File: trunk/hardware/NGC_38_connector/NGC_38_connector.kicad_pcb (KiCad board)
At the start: 2 copper layers, 38 x 29 mm, 5 parts, among them P1 DIL38, P2 CONN_10, P3 CONN_9, P4 CONN_10, P5 CONN_9

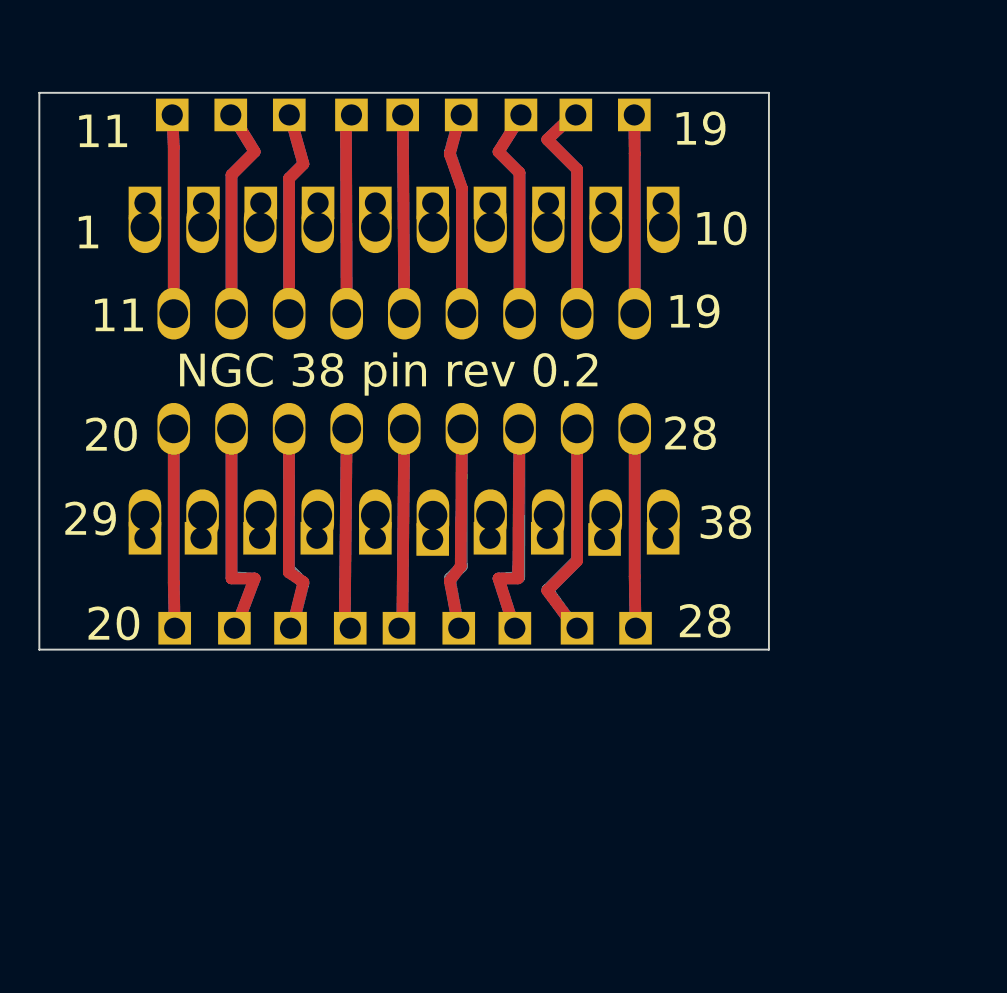
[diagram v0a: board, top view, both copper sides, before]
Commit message: 
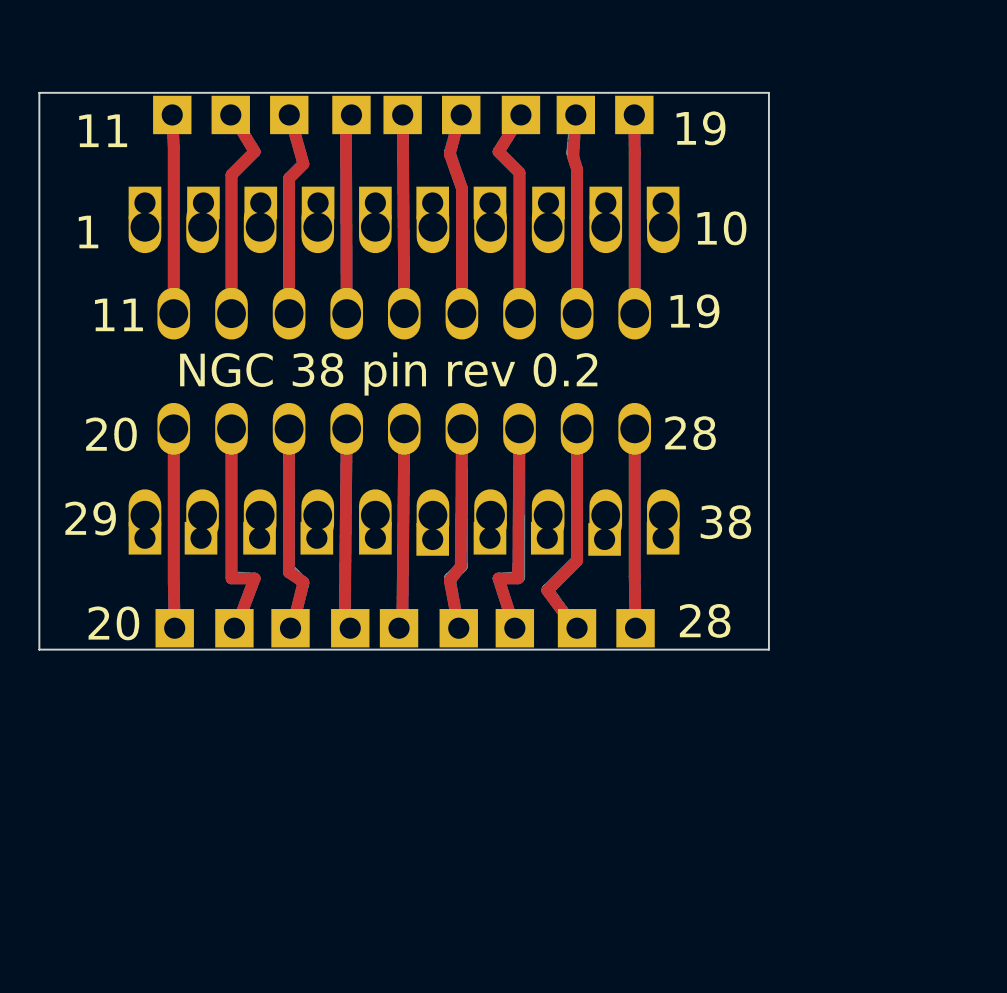
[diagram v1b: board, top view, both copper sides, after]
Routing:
- net N-0000013: track 23.5 -> 21.0 mm
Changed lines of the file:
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@@
     (links 38)
     (no_connects 0)
-    (area 130.949999 132.969 169.050001 165.061901)
+    (area 130.949999 132.969 169.050001 165.053714)
     (thickness 1.6)
     (drawings 30)
@@
     (mod_text_size 1 1)
     (mod_text_width 0.15)
-    (pad_size 1.7 1.7)
+    (pad_size 2 2)
     (pad_drill 1.1)
     (pad_to_mask_clearance 0)
@@
       (effects (font (size 1.524 1.016) (thickness 0.254)))
     )
-    (pad 1 thru_hole rect (at -11.684 0) (size 1.7 1.7) (drill 1.1)
+    (pad 1 thru_hole rect (at -11.684 0) (size 2 2) (drill 1.1)
       (layers *.Cu *.Mask F.SilkS)
       (net 8 N-0000016)
     )
-    (pad 2 thru_hole rect (at -8.5725 0) (size 1.7 1.7) (drill 1.1)
+    (pad 2 thru_hole rect (at -8.5725 0) (size 2 2) (drill 1.1)
       (layers *.Cu *.Mask F.SilkS)
       (net 21 N-0000028)
     )
-    (pad 3 thru_hole rect (at -5.6515 0) (size 1.7 1.7) (drill 1.1)
+    (pad 3 thru_hole rect (at -5.6515 0) (size 2 2) (drill 1.1)
       (layers *.Cu *.Mask F.SilkS)
       (net 20 N-0000027)
     )
-    (pad 4 thru_hole rect (at -2.54 0) (size 1.7 1.7) (drill 1.1)
+    (pad 4 thru_hole rect (at -2.54 0) (size 2 2) (drill 1.1)
       (layers *.Cu *.Mask F.SilkS)
       (net 19 N-0000026)
     )
-    (pad 5 thru_hole rect (at 0 0) (size 1.7 1.7) (drill 1.1)
+    (pad 5 thru_hole rect (at 0 0) (size 2 2) (drill 1.1)
       (layers *.Cu *.Mask F.SilkS)
       (net 18 N-0000025)
     )
-    (pad 6 thru_hole rect (at 3.1115 0) (size 1.7 1.7) (drill 1.1)
+    (pad 6 thru_hole rect (at 3.1115 0) (size 2 2) (drill 1.1)
       (layers *.Cu *.Mask F.SilkS)
       (net 17 N-0000024)
     )
-    (pad 7 thru_hole rect (at 6.0325 0) (size 1.7 1.7) (drill 1.1)
+    (pad 7 thru_hole rect (at 6.0325 0) (size 2 2) (drill 1.1)
       (layers *.Cu *.Mask F.SilkS)
       (net 16 N-0000023)
     )
-    (pad 8 thru_hole rect (at 9.271 0) (size 1.7 1.7) (drill 1.1)
+    (pad 8 thru_hole rect (at 9.271 0) (size 2 2) (drill 1.1)
       (layers *.Cu *.Mask F.SilkS)
       (net 15 N-0000022)
     )
-    (pad 9 thru_hole rect (at 12.319 0) (size 1.7 1.7) (drill 1.1)
+    (pad 9 thru_hole rect (at 12.319 0) (size 2 2) (drill 1.1)
       (layers *.Cu *.Mask F.SilkS)
       (net 14 N-0000021)
@@
       (effects (font (size 1.524 1.016) (thickness 0.254)))
     )
-    (pad 1 thru_hole rect (at -11.8745 0) (size 1.7 1.7) (drill 1.1)
+    (pad 1 thru_hole rect (at -11.8745 0) (size 2 2) (drill 1.1)
       (layers *.Cu *.Mask F.SilkS)
       (net 13 N-0000020)
     )
-    (pad 2 thru_hole rect (at -8.8265 0) (size 1.7 1.7) (drill 1.1)
+    (pad 2 thru_hole rect (at -8.8265 0) (size 2 2) (drill 1.1)
       (layers *.Cu *.Mask F.SilkS)
       (net 11 N-0000019)
     )
-    (pad 3 thru_hole rect (at -5.7785 0) (size 1.7 1.7) (drill 1.1)
+    (pad 3 thru_hole rect (at -5.7785 0) (size 2 2) (drill 1.1)
       (layers *.Cu *.Mask F.SilkS)
       (net 10 N-0000018)
     )
-    (pad 4 thru_hole rect (at -2.54 0) (size 1.7 1.7) (drill 1.1)
+    (pad 4 thru_hole rect (at -2.54 0) (size 2 2) (drill 1.1)
       (layers *.Cu *.Mask F.SilkS)
       (net 9 N-0000017)
     )
-    (pad 5 thru_hole rect (at 0.127 0) (size 1.7 1.7) (drill 1.1)
+    (pad 5 thru_hole rect (at 0.127 0) (size 2 2) (drill 1.1)
       (layers *.Cu *.Mask F.SilkS)
       (net 1 N-000001)
     )
-    (pad 6 thru_hole rect (at 3.175 0) (size 1.7 1.7) (drill 1.1)
+    (pad 6 thru_hole rect (at 3.175 0) (size 2 2) (drill 1.1)
       (layers *.Cu *.Mask F.SilkS)
       (net 7 N-0000015)
     )
-    (pad 7 thru_hole rect (at 6.2865 0) (size 1.7 1.7) (drill 1.1)
+    (pad 7 thru_hole rect (at 6.2865 0) (size 2 2) (drill 1.1)
       (layers *.Cu *.Mask F.SilkS)
       (net 6 N-0000014)
     )
-    (pad 8 thru_hole rect (at 9.144 0) (size 1.7 1.7) (drill 1.1)
+    (pad 8 thru_hole rect (at 9.144 0) (size 2 2) (drill 1.1)
       (layers *.Cu *.Mask F.SilkS)
       (net 5 N-0000013)
     )
-    (pad 9 thru_hole rect (at 12.192 0) (size 1.7 1.7) (drill 1.1)
+    (pad 9 thru_hole rect (at 12.192 0) (size 2 2) (drill 1.1)
       (layers *.Cu *.Mask F.SilkS)
       (net 4 N-0000012)
@@
   (segment (start 162.008 138.678) (end 161.9885 136.5885) (width 0.6096) (layer B.Cu) (net 4) (status 20))
   (segment (start 159.008 147) (end 159.008 139.488) (width 0.6096) (layer F.Cu) (net 5))
-  (segment (start 159.008 139.488) (end 157.455 137.935) (width 0.6096) (layer F.Cu) (net 5))
-  (segment (start 157.455 137.935) (end 158.9405 136.525) (width 0.6096) (layer F.Cu) (net 5) (status 20))
+  (segment (start 159.008 139.488) (end 158.8135 138.8745) (width 0.6096) (layer F.Cu) (net 5))
+  (segment (start 158.8135 138.8745) (end 158.9405 136.525) (width 0.6096) (layer F.Cu) (net 5) (status 20))
   (segment (start 159.008 147) (end 159.008 139.488) (width 0.6096) (layer B.Cu) (net 5))
-  (segment (start 157.455 137.935) (end 158.9405 136.525) (width 0.6096) (layer B.Cu) (net 5) (status 20))
-  (segment (start 159.008 139.488) (end 157.455 137.935) (width 0.6096) (layer B.Cu) (net 5))
+  (segment (start 158.75 138.6205) (end 158.9405 136.525) (width 0.6096) (layer B.Cu) (net 5) (status 20))
+  (segment (start 159.008 139.488) (end 158.75 138.6205) (width 0.6096) (layer B.Cu) (net 5))
   (segment (start 156.008 147) (end 156.008 139.663) (width 0.6096) (layer F.Cu) (net 6))
   (segment (start 156.008 139.663) (end 154.915 138.57) (width 0.6096) (layer F.Cu) (net 6))

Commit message: 0.3
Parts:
- moved P4 0.88 mm to (149.3, 159.6)
- moved P2 0.78 mm to (149.7, 140.5)
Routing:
- net N-0000022: track 23.3 -> 21.0 mm
- net N-0000023: track 23.2 -> 20.9 mm
- net N-0000036: track 0.00 -> 2.15 mm
- net N-0000030: track 0.00 -> 2.14 mm
- net N-0000034: track 0.00 -> 2.10 mm
- net N-0000031: track 0.00 -> 2.09 mm
- net N-0000035: track 0.00 -> 2.09 mm
- net N-0000032: track 0.00 -> 2.08 mm
- net N-0000037: track 0.00 -> 2.08 mm
- net N-0000033: track 0.00 -> 2.08 mm
- net N-0000029: track 0.00 -> 2.08 mm
- net N-0000038: track 0.00 -> 2.08 mm
- net N-0000010: track 0.00 -> 2.07 mm
- net N-000009: track 0.00 -> 2.06 mm
- net N-000004: track 0.00 -> 2.06 mm
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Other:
- board text added: "NGC 38 pin rev 0.3"
- board text removed: "NGC 38 pin rev 0.2"

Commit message: 4.0.1
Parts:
- added P6: CONN_10, SIL-10, F.Cu at (163.2, 134.6)
- added P7: CONN_9, SIL-9, F.Cu at (163.2, 141.0)
- added P8: CONN_9, SIL-9, F.Cu at (163.2, 172.1)
- added P9: CONN_10, SIL-10, F.Cu at (163.2, 178.4)
- moved P4 21.4 mm to (163.2, 175.9)
- moved P3 15.1 mm to (163.2, 143.5)
- moved P1 15.0 mm to (149.9, 156.8)
- moved P5 14.8 mm to (163.2, 169.5)
- moved P2 13.9 mm to (163.2, 137.2)
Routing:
- net N-0000010: track 2.04 -> 31.3 mm
- net N-000001: track 2.05 -> 31.0 mm
- net N-000009: track 2.05 -> 30.9 mm
- net N-000002: track 2.07 -> 30.6 mm
- net N-000008: track 2.06 -> 30.5 mm
- net N-000003: track 2.06 -> 30.3 mm
- net N-000007: track 2.04 -> 30.2 mm
- net N-0000035: track 2.08 -> 30.0 mm
- net N-000004: track 2.06 -> 29.9 mm
- net N-000006: track 2.04 -> 29.8 mm
- net N-0000027: track 2.09 -> 29.8 mm
- net N-0000034: track 2.15 -> 29.7 mm
- net N-000005: track 2.05 -> 29.5 mm
- net N-0000028: track 2.10 -> 29.4 mm
- net N-0000033: track 2.08 -> 29.3 mm
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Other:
- board size 38 x 29 mm -> 31.8 x 47.6 mm
- board text added: "NGC 38 pin rev 0.1"
- board text removed: "NGC 38 pin rev 0.3"

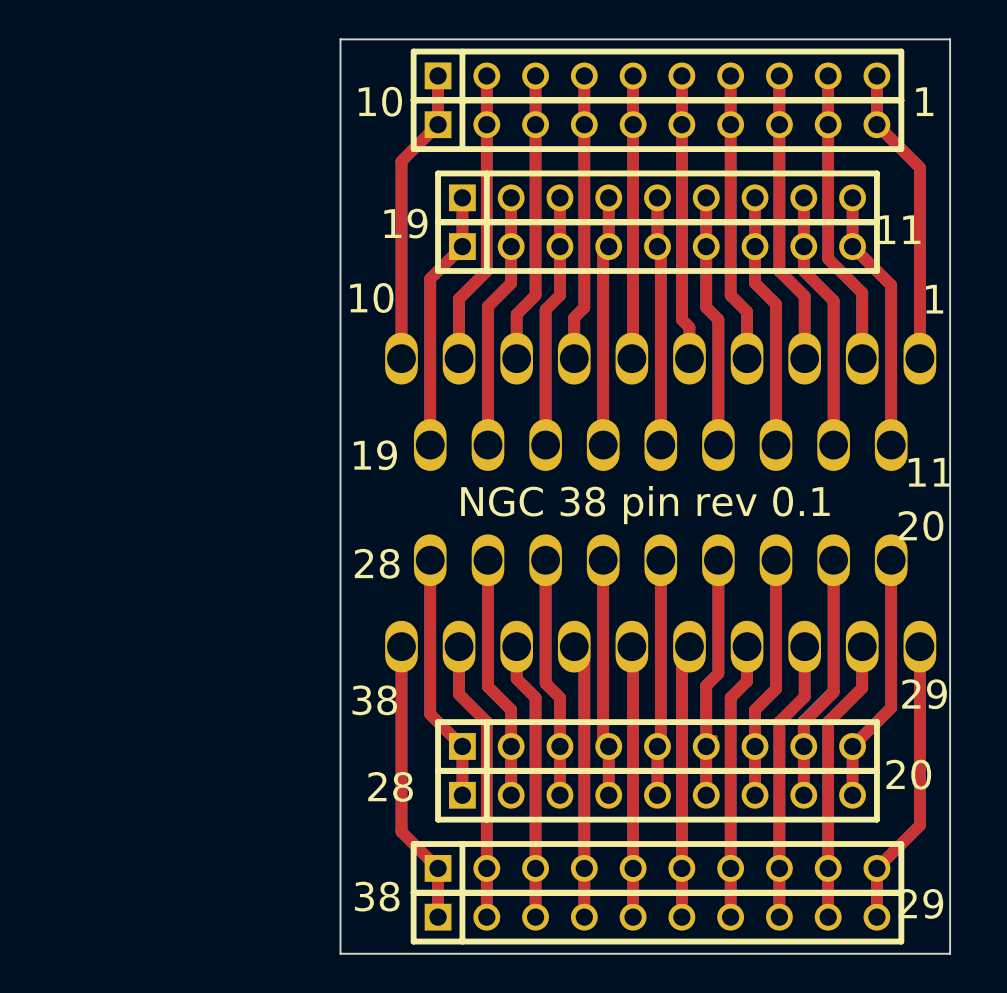
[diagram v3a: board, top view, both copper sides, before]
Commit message: a bit larger holes for the wires
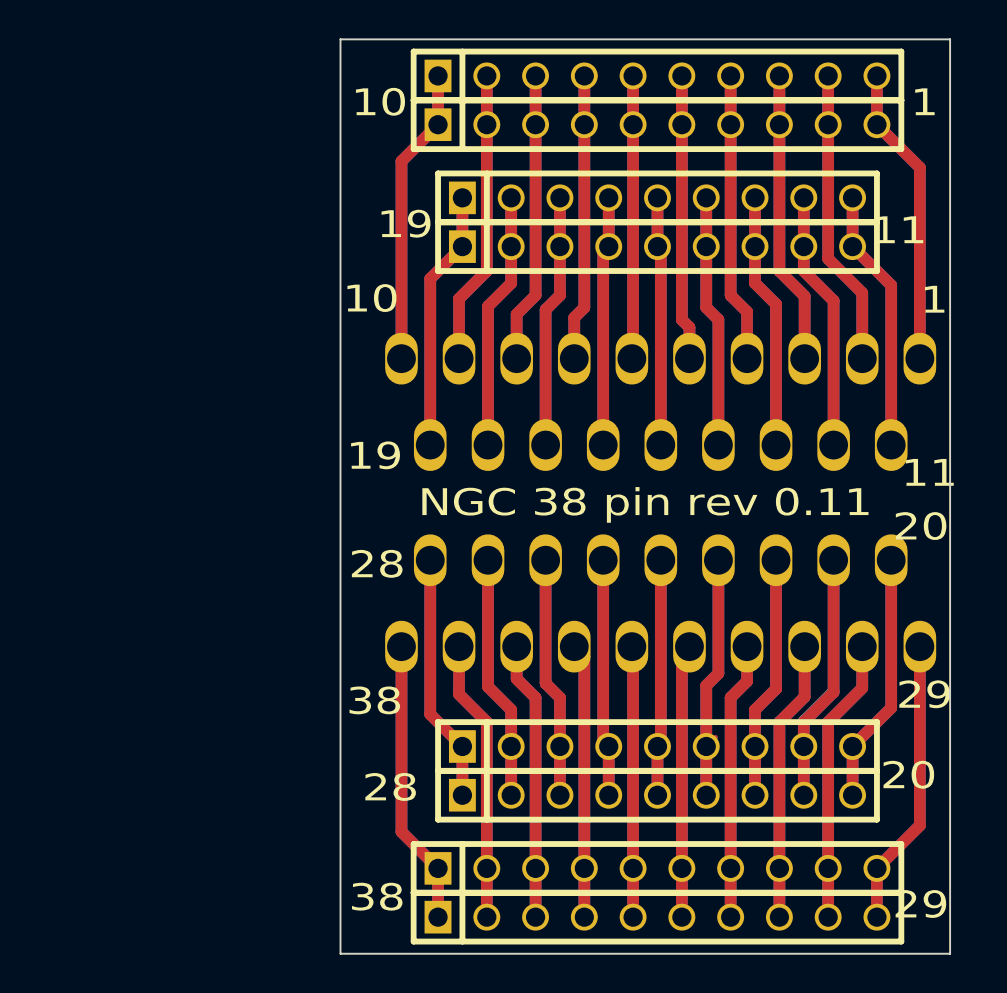
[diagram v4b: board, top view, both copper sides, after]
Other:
- board text added: "NGC 38 pin rev 0.11"
- board text removed: "NGC 38 pin rev 0.1"

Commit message: new version
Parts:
- removed P6, P9: CONN_10, SIL-10
- removed P7, P8: CONN_9, SIL-9
- moved P2 0.34 mm to (163.1, 136.8)
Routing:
- net N-0000011: track 31.0 -> 0.00 mm
- net N-0000010: track 30.6 -> 0.00 mm
- net N-000009: track 30.3 -> 0.00 mm
- net N-0000028: track 25.5 -> 20.4 mm
- net N-0000027: track 25.1 -> 20.0 mm
- net N-0000026: track 25.3 -> 20.3 mm
- net N-0000025: track 24.6 -> 19.6 mm
- net N-0000024: track 25.7 -> 20.6 mm
- net N-0000023: track 25.4 -> 20.3 mm
- net N-0000022: track 25.8 -> 20.7 mm
- net N-0000021: track 26.1 -> 21.1 mm
- net N-0000016: track 25.9 -> 20.8 mm
- net N-000008: track 29.9 -> 24.8 mm
- net N-000007: track 29.5 -> 24.4 mm
- net N-000006: track 29.8 -> 24.7 mm
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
